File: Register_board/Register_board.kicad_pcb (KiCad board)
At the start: 2 copper layers, 124 x 83 mm, 26 parts, among them J1 Conn_02x32_Odd_Even, U1 74LS374, U10 74LS181, U11 74LS181, U12 74LS374, U13 74LS374, U14 74LS374, U15 74LS374, U16 74LS244, U2 74LS374, U3 74LS374, U4 74LS374, U5 74LS244, U6 74LS374, U7 74LS374, U8 74LS244, U9 74LS75

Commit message: Register board and Control panel ordered
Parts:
- RN1, RN2, RN3, RN4: value R_Network08 -> 10K
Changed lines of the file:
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@@
     (property "ki_description" "Arithmetic logic unit")
     (property "ki_keywords" "TTL ALU ARITH")
-    (attr through_hole)
+    (attr through_hole exclude_from_pos_files)
     (fp_text reference "U11" (at 19.05 28.58) (layer "F.SilkS")
         (effects (font (size 1 1) (thickness 0.15)))
@@
     (property "ki_description" "8-bit Register, 3-state outputs")
     (property "ki_keywords" "TTL DFF DFF8 REG 3State")
-    (attr through_hole)
+    (attr through_hole exclude_from_pos_files)
     (fp_text reference "U1" (at 3.937 25.527) (layer "F.SilkS")
         (effects (font (size 1 1) (thickness 0.15)))
@@
     (property "ki_description" "8-bit Register, 3-state outputs")
     (property "ki_keywords" "TTL DFF DFF8 REG 3State")
-    (attr through_hole)
+    (attr through_hole exclude_from_pos_files)
     (fp_text reference "U15" (at 3.81 25.654) (layer "F.SilkS")
         (effects (font (size 1 1) (thickness 0.15)))
@@
     (property "ki_description" "8 resistor network, star topology, bussed resistors, small symbol")
     (property "ki_keywords" "R network star-topology")
-    (attr through_hole)
+    (attr through_hole exclude_from_pos_files)
     (fp_text reference "RN4" (at -3.175 0) (layer "F.SilkS")
         (effects (font (size 1 1) (thickness 0.15)))
     )
-    (fp_text value "R_Network08" (at 11.43 2.4) (layer "F.Fab")
+    (fp_text value "10K" (at 11.43 2.4) (layer "F.Fab")
         (effects (font (size 1 1) (thickness 0.15)))
     )
@@
     (property "ki_description" "Mounting Hole without connection")
     (property "ki_keywords" "mounting hole")
-    (attr exclude_from_pos_files)
+    (attr exclude_from_pos_files exclude_from_bom)
     (fp_text reference "H1" (at 0 -4.5) (layer "F.SilkS") hide
         (effects (font (size 1 1) (thickness 0.15)))
@@
     (property "ki_description" "8-bit Register, 3-state outputs")
     (property "ki_keywords" "TTL DFF DFF8 REG 3State")
-    (attr through_hole)
+    (attr through_hole exclude_from_pos_files)
     (fp_text reference "U12" (at 3.81 25.654) (layer "F.SilkS")
         (effects (font (size 1 1) (thickness 0.15)))
@@
     (property "ki_description" "8-bit Register, 3-state outputs")
     (property "ki_keywords" "TTL DFF DFF8 REG 3State")
-    (attr through_hole)
+    (attr through_hole exclude_from_pos_files)
     (fp_text reference "U6" (at 0.127 25.527) (layer "F.SilkS")
         (effects (font (size 1 1) (thickness 0.15)))
@@
     (property "ki_description" "8-bit Register, 3-state outputs")
     (property "ki_keywords" "TTL DFF DFF8 REG 3State")
-    (attr through_hole)
+    (attr through_hole exclude_from_pos_files)
     (fp_text reference "U7" (at 7.493 25.527) (layer "F.SilkS")
         (effects (font (size 1 1) (thickness 0.15)))
@@
     (property "ki_description" "Generic connector, double row, 02x32, odd/even pin numbering scheme (row 1 odd numbers, row 2 even numbers), script generated (kicad-library-utils/schlib/autogen/connector/)")
     (property "ki_keywords" "connector")
-    (attr through_hole)
+    (attr through_hole exclude_from_pos_files)
     (fp_text reference "J1" (at 1.27 -6.1 -90) (layer "F.SilkS")
         (effects (font (size 1 1) (thickness 0.15)))
@@
     (fp_line (start 5.72 83.84) (end -3.18 83.84)
       (stroke (width 0.1) (type solid)) (layer "F.Fab"))
-    (pad "1" thru_hole roundrect (at 0 0 270) (size 1.7 1.7) (drill 1) (layers "*.Cu" "*.Mask") (roundrect_rratio 0.147059)
+    (pad "1" thru_hole roundrect (at 0 0 270) (size 1.7 1.7) (drill 1) (layers "*.Cu" "*.Mask") (roundrect_rratio 0.1470588235)
       (net 11 "GND") (pinfunction "Pin_1") (pintype "passive"))
     (pad "2" thru_hole circle (at 2.54 0 270) (size 1.7 1.7) (drill 1) (layers "*.Cu" "*.Mask")
@@
     (property "ki_description" "8-bit Register, 3-state outputs")
     (property "ki_keywords" "TTL DFF DFF8 REG 3State")
-    (attr through_hole)
+    (attr through_hole exclude_from_pos_files)
     (fp_text reference "U13" (at 3.81 25.654) (layer "F.SilkS")
         (effects (font (size 1 1) (thickness 0.15)))
@@
     (property "ki_description" "8 resistor network, star topology, bussed resistors, small symbol")
     (property "ki_keywords" "R network star-topology")
-    (attr through_hole)
+    (attr through_hole exclude_from_pos_files)
     (fp_text reference "RN2" (at -2.54 0.127 180) (layer "F.SilkS")
         (effects (font (size 1 1) (thickness 0.15)))
     )
-    (fp_text value "R_Network08" (at 11.43 2.4 90) (layer "F.Fab")
+    (fp_text value "10K" (at 11.43 2.4 90) (layer "F.Fab")
         (effects (font (size 1 1) (thickness 0.15)))
     )
@@
     (property "ki_description" "8-bit Register, 3-state outputs")
     (property "ki_keywords" "TTL DFF DFF8 REG 3State")
-    (attr through_hole)
+    (attr through_hole exclude_from_pos_files)
     (fp_text reference "U4" (at 3.81 25.527) (layer "F.SilkS")
         (effects (font (size 1 1) (thickness 0.15)))
@@
     (property "ki_description" "8-bit Register, 3-state outputs")
     (property "ki_keywords" "TTL DFF DFF8 REG 3State")
-    (attr through_hole)
+    (attr through_hole exclude_from_pos_files)
     (fp_text reference "U3" (at 3.8 25.527) (layer "F.SilkS")
         (effects (font (size 1 1) (thickness 0.15)))
@@
     (property "ki_description" "Octal Buffer and Line Driver With 3-State Output, active-low enables, non-inverting outputs")
     (property "ki_keywords" "7400 logic ttl low power schottky")
-    (attr through_hole)
+    (attr through_hole exclude_from_pos_files)
     (fp_text reference "U5" (at 3.175 25.527) (layer "F.SilkS")
         (effects (font (size 1 1) (thickness 0.15)))
@@
     (property "ki_description" "Octal Buffer and Line Driver With 3-State Output, active-low enables, non-inverting outputs")
     (property "ki_keywords" "7400 logic ttl low power schottky")
-    (attr through_hole)
+    (attr through_hole exclude_from_pos_files)
     (fp_text reference "U16" (at 3.81 25.654) (layer "F.SilkS")
         (effects (font (size 1 1) (thickness 0.15)))
@@
     (property "ki_description" "8-bit Register, 3-state outputs")
     (property "ki_keywords" "TTL DFF DFF8 REG 3State")
-    (attr through_hole)
+    (attr through_hole exclude_from_pos_files)
     (fp_text reference "U14" (at 3.937 25.654) (layer "F.SilkS")
         (effects (font (size 1 1) (thickness 0.15)))
@@
     (property "ki_description" "Octal Buffer and Line Driver With 3-State Output, active-low enables, non-inverting outputs")
     (property "ki_keywords" "7400 logic ttl low power schottky")
-    (attr through_hole)
+    (attr through_hole exclude_from_pos_files)
     (fp_text reference "U8" (at 0.127 25.527) (layer "F.SilkS")
         (effects (font (size 1 1) (thickness 0.15)))
@@
     (property "ki_description" "Mounting Hole without connection")
     (property "ki_keywords" "mounting hole")
-    (attr exclude_from_pos_files)
+    (attr exclude_from_pos_files exclude_from_bom)
     (fp_text reference "H4" (at 0 -4.5) (layer "F.SilkS")
         (effects (font (size 1 1) (thickness 0.15)))
@@
     (property "ki_description" "8 resistor network, star topology, bussed resistors, small symbol")
     (property "ki_keywords" "R network star-topology")
-    (attr through_hole)
+    (attr through_hole exclude_from_pos_files)
     (fp_text reference "RN3" (at -3.175 0) (layer "F.SilkS")
         (effects (font (size 1 1) (thickness 0.15)))
     )
-    (fp_text value "R_Network08" (at 11.43 2.4) (layer "F.Fab")
+    (fp_text value "10K" (at 11.43 2.4) (layer "F.Fab")
         (effects (font (size 1 1) (thickness 0.15)))
     )
@@
     (property "ki_description" "Mounting Hole without connection")
     (property "ki_keywords" "mounting hole")
-    (attr exclude_from_pos_files)
+    (attr exclude_from_pos_files exclude_from_bom)
     (fp_text reference "H3" (at 0 -4.5) (layer "F.SilkS") hide
         (effects (font (size 1 1) (thickness 0.15)))
@@
     (property "ki_description" "8 resistor network, star topology, bussed resistors, small symbol")
     (property "ki_keywords" "R network star-topology")
-    (attr through_hole)
+    (attr through_hole exclude_from_pos_files)
     (fp_text reference "RN1" (at -2.413 0.127 180) (layer "F.SilkS")
         (effects (font (size 1 1) (thickness 0.15)))
     )
-    (fp_text value "R_Network08" (at 11.43 2.4 90) (layer "F.Fab")
+    (fp_text value "10K" (at 11.43 2.4 90) (layer "F.Fab")
         (effects (font (size 1 1) (thickness 0.15)))
     )
@@
     (property "ki_description" "8-bit Register, 3-state outputs")
     (property "ki_keywords" "TTL DFF DFF8 REG 3State")
-    (attr through_hole)
+    (attr through_hole exclude_from_pos_files)
     (fp_text reference "U2" (at 3.165 25.527) (layer "F.SilkS")
         (effects (font (size 1 1) (thickness 0.15)))
@@
     (property "ki_description" "4-bit Latch")
     (property "ki_keywords" "TTL DFF Latch")
-    (attr through_hole)
+    (attr through_hole exclude_from_pos_files)
     (fp_text reference "U9" (at 7.62 20.32) (layer "F.SilkS")
         (effects (font (size 1 1) (thickness 0.15)))
@@
     (property "ki_description" "Arithmetic logic unit")
     (property "ki_keywords" "TTL ALU ARITH")
-    (attr through_hole)
+    (attr through_hole exclude_from_pos_files)
     (fp_text reference "U10" (at 19.05 28.575) (layer "F.SilkS")
         (effects (font (size 1 1) (thickness 0.15)))
@@
     (property "ki_description" "Mounting Hole without connection")
     (property "ki_keywords" "mounting hole")
-    (attr exclude_from_pos_files)
+    (attr exclude_from_pos_files exclude_from_bom)
     (fp_text reference "H2" (at 0 -4.5) (layer "F.SilkS") hide
         (effects (font (size 1 1) (thickness 0.15)))

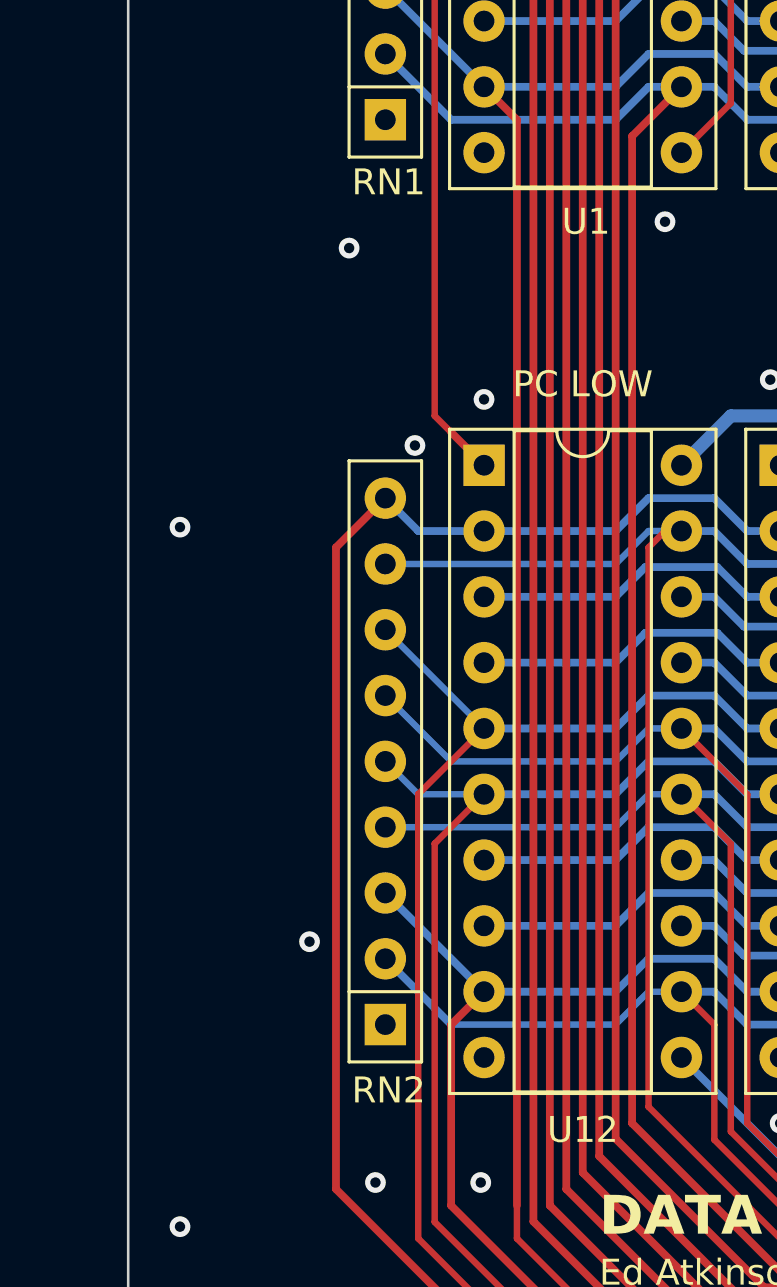
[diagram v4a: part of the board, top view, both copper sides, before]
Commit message: Fix address line labelling error
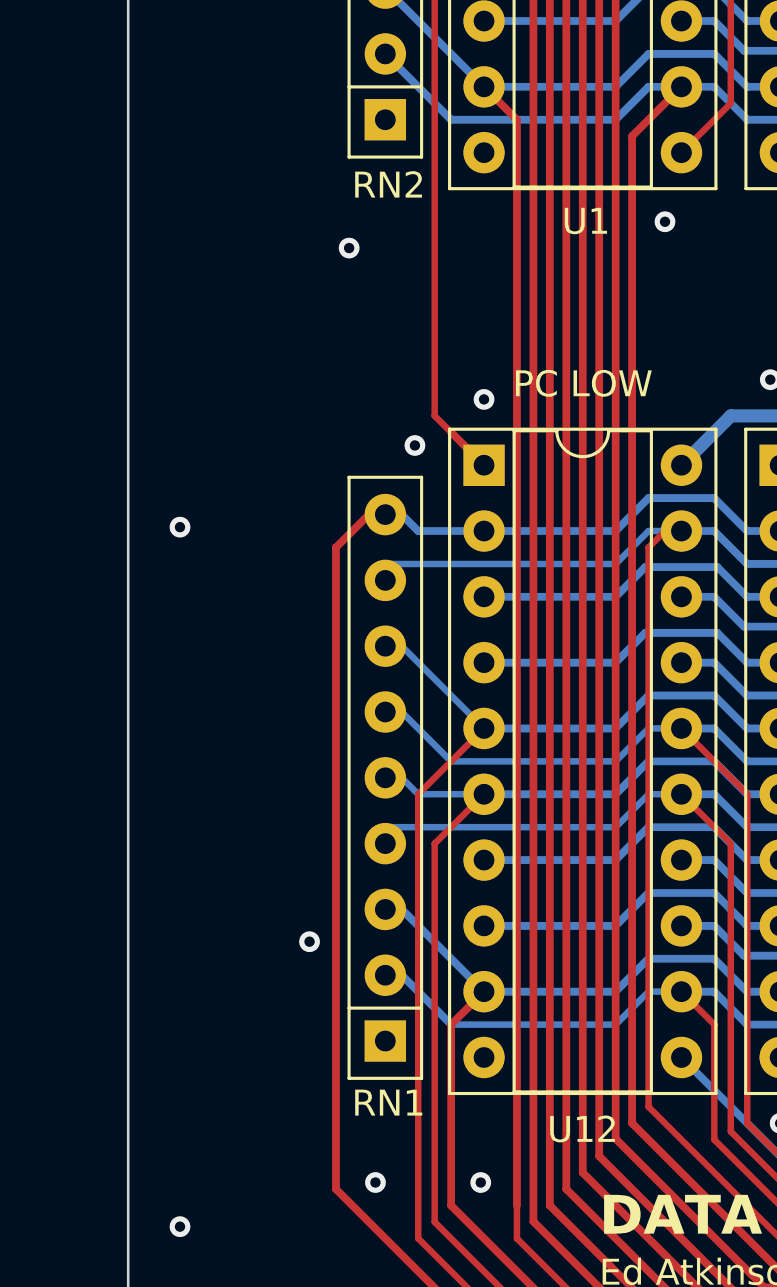
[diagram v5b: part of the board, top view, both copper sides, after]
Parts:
- moved RN1 35.6 mm to (61.0, 106.0)
- moved RN2 34.9 mm to (61.0, 70.5)
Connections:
- J1 pad 49: /A14 -> /A6
- J1 pad 50: /A13 -> /A5
- J1 pad 51: /A12 -> /A4
- J1 pad 52: /A15 -> /A7
- J1 pad 53: /A4 -> /A12
- J1 pad 54: /A5 -> /A13
- J1 pad 55: /A6 -> /A14
- J1 pad 56: /A7 -> /A15
- J1 pad 57: /A0 -> /A8
- J1 pad 58: /A8 -> /A0
- J1 pad 59: /A1 -> /A9
- J1 pad 60: /A9 -> /A1
- J1 pad 61: /A2 -> /A10
- J1 pad 62: /A10 -> /A2
- J1 pad 63: /A3 -> /A11
- J1 pad 64: /A11 -> /A3
- U1 pad 12: /A4 -> /A12
- U1 pad 15: /A5 -> /A13
- U1 pad 16: /A6 -> /A14
- U1 pad 19: /A7 -> /A15
- U1 pad 2: /A0 -> /A8
- U1 pad 5: /A1 -> /A9
- U1 pad 6: /A2 -> /A10
- U1 pad 9: /A3 -> /A11
- U12 pad 12: /A12 -> /A4
- U12 pad 15: /A13 -> /A5
- U12 pad 16: /A14 -> /A6
- U12 pad 19: /A15 -> /A7
- U12 pad 2: /A8 -> /A0
- U12 pad 5: /A9 -> /A1
- U12 pad 6: /A10 -> /A2
- U12 pad 9: /A11 -> /A3
- U13 pad 12: /A12 -> /A4
- U13 pad 15: /A13 -> /A5
- U13 pad 16: /A14 -> /A6
- U13 pad 19: /A15 -> /A7
- U13 pad 2: /A8 -> /A0
- U13 pad 5: /A9 -> /A1
- U13 pad 6: /A10 -> /A2
- U13 pad 9: /A11 -> /A3
- U14 pad 12: /A12 -> /A4
- U14 pad 15: /A13 -> /A5
- U14 pad 16: /A14 -> /A6
- U14 pad 19: /A15 -> /A7
- U14 pad 2: /A8 -> /A0
- U14 pad 5: /A9 -> /A1
- U14 pad 6: /A10 -> /A2
- U14 pad 9: /A11 -> /A3
- U15 pad 12: /A12 -> /A4
- U15 pad 15: /A13 -> /A5
- U15 pad 16: /A14 -> /A6
- U15 pad 19: /A15 -> /A7
- U15 pad 2: /A8 -> /A0
- U15 pad 5: /A9 -> /A1
- U15 pad 6: /A10 -> /A2
- U15 pad 9: /A11 -> /A3
- U16 pad 11: /A12 -> /A4
- U16 pad 13: /A13 -> /A5
- U16 pad 15: /A14 -> /A6
- U16 pad 17: /A15 -> /A7
- U16 pad 2: /A8 -> /A0
- U16 pad 4: /A9 -> /A1
- U16 pad 6: /A10 -> /A2
- U16 pad 8: /A11 -> /A3
- U2 pad 12: /A4 -> /A12
- U2 pad 15: /A5 -> /A13
- U2 pad 16: /A6 -> /A14
- U2 pad 19: /A7 -> /A15
- U2 pad 2: /A0 -> /A8
- U2 pad 5: /A1 -> /A9
- U2 pad 6: /A2 -> /A10
- U2 pad 9: /A3 -> /A11
- U3 pad 12: /A4 -> /A12
- U3 pad 15: /A5 -> /A13
- U3 pad 16: /A6 -> /A14
- U3 pad 19: /A7 -> /A15
- U3 pad 2: /A0 -> /A8
- U3 pad 5: /A1 -> /A9
- U3 pad 6: /A2 -> /A10
- U3 pad 9: /A3 -> /A11
- U4 pad 12: /A4 -> /A12
- U4 pad 15: /A5 -> /A13
- U4 pad 16: /A6 -> /A14
- U4 pad 19: /A7 -> /A15
- U4 pad 2: /A0 -> /A8
- U4 pad 5: /A1 -> /A9
- U4 pad 6: /A2 -> /A10
- U4 pad 9: /A3 -> /A11
- U5 pad 11: /A4 -> /A12
- U5 pad 13: /A5 -> /A13
- U5 pad 15: /A6 -> /A14
- U5 pad 17: /A7 -> /A15
- U5 pad 2: /A0 -> /A8
- U5 pad 4: /A1 -> /A9
- U5 pad 6: /A2 -> /A10
- U5 pad 8: /A3 -> /A11
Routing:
- net /A4: track 125.1 -> 89.7 mm
- net /A12: track 89.7 -> 125.1 mm
- net /A5: track 137.3 -> 102.5 mm
- net /A13: track 102.5 -> 137.3 mm
- net /A7: track 146.0 -> 111.4 mm
- net /A15: track 111.4 -> 146.0 mm
- net /A6: track 135.3 -> 101.9 mm
- net /A14: track 101.9 -> 135.3 mm
- net /A3: track 111.2 -> 78.5 mm
- net /A11: track 78.5 -> 111.2 mm
- net /A2: track 119.6 -> 90.6 mm
- net /A10: track 90.6 -> 119.6 mm
- net /A9: track 98.5 -> 125.0 mm
- net /A1: track 125.0 -> 98.5 mm
- net /A8: track 111.2 -> 133.3 mm
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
